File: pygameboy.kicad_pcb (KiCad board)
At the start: 2 copper layers, 49.3 x 59.7 mm, 135 parts, among them J1 Conn_01x01, J2 Conn_01x01, J4 USB_C_Receptacle_USB2.0_16P, J5 MIDI IN, J6 MIDI OUT, Q1 BSS138, SW1 SW_Push, U1 CARTRIDGE, U10 RP2350_80QFN, U2 W25Q128JVS, U5 74x4245, U7 AP2204K-3.3, U8 H11L1, Y1 ABM8-272-T3

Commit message: Ordered!
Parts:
- removed C1, C11, C18, C19, C20, C21, C22, C23, C24, C25, C26, C27: 100n, Capacitor_SMD:C_0402_1005Metric
- removed the C13 at (134.0, 72.9)
- removed C14, C15: 4.7u, Capacitor_SMD:C_0402_1005Metric
- removed C3, C4: 15p, Capacitor_SMD:C_0402_1005Metric
- removed C6: 4.7u, RP2350_80QFN_minimal:C_0402_1005Metric_small_pads
- removed the C7 at (189.7, 39.5)
- removed L1: 3.3u, RP2350_80QFN_minimal:L_pol_2016
- removed R12: DNF, Resistor_SMD:R_0402_1005Metric
- removed R14, R16: 1k, Resistor_SMD:R_0402_1005Metric
- removed R15: 33, Resistor_SMD:R_0402_1005Metric
- removed R17, R18: 27, Resistor_SMD:R_0402_1005Metric
- removed the R2 at (185.4, 45.5)
- removed the R3 at (185.7, 41.1)
- removed TP36: SAMD_RESET, keystone:5015-SMT-TestPoint
- removed Y1: ABM8-272-T3, Crystal:Crystal_SMD_3225-4Pin_3.2x2.5mm
- added C2: 47uF, Capacitor_SMD:C_0805_2012Metric, F.Cu at (146.3, 65.2)
- added C201: 100n, Capacitor_SMD:C_0402_1005Metric, F.Cu at (133.8, 50.6)
- added C202: 15p, Capacitor_SMD:C_0402_1005Metric, F.Cu at (133.9, 75.0)
- added C203: 15p, Capacitor_SMD:C_0402_1005Metric, F.Cu at (136.9, 75.0)
- added C204: 4.7u, RP2350_80QFN_minimal:C_0402_1005Metric_small_pads, F.Cu at (138.3, 58.5)
- added C205: 4.7u, RP2350_80QFN_minimal:C_0402_1005Metric_small_pads, F.Cu at (138.3, 57.5)
- added C206: 100n, Capacitor_SMD:C_0402_1005Metric, F.Cu at (143.3, 64.1)
- added C207: 4.7u, Capacitor_SMD:C_0402_1005Metric, F.Cu at (140.6, 57.8)
- added C210: 100n, Capacitor_SMD:C_0402_1005Metric, F.Cu at (142.9, 60.3)
- added C212: 100n, Capacitor_SMD:C_0402_1005Metric, F.Cu at (141.8, 70.5)
- added C214: 100n, Capacitor_SMD:C_0402_1005Metric, F.Cu at (129.1, 56.0)
- added C215: 100n, Capacitor_SMD:C_0402_1005Metric, F.Cu at (127.3, 61.7)
- added C216: 100n, Capacitor_SMD:C_0402_1005Metric, F.Cu at (134.2, 55.8)
- added C217: 100n, Capacitor_SMD:C_0402_1005Metric, F.Cu at (134.2, 71.3)
- added C218: 100n, Capacitor_SMD:C_0402_1005Metric, F.Cu at (132.7, 71.3)
- added J14: Conn_01x04, Connector_JST:JST_SH_SM04B-SRSS-TB_1x04-1MP_P1.00mm_Horizontal, F.Cu at (138.0, 41.5)
- added L201: 3.3u, RP2350_80QFN_minimal:L_pol_2016, F.Cu at (138.3, 56.0)
- added R11: 10k, Resistor_SMD:R_0402_1005Metric, F.Cu at (146.8, 83.8)
- added R201: 10k, Resistor_SMD:R_0402_1005Metric, F.Cu at (124.8, 48.4)
- added R202: 1k, Resistor_SMD:R_0402_1005Metric, F.Cu at (135.6, 72.9)
- added R203: 33, Resistor_SMD:R_0402_1005Metric, F.Cu at (140.6, 55.9)
- added R204: 1k, Resistor_SMD:R_0402_1005Metric, F.Cu at (146.1, 51.4)
- added SW2: SW_Push, Button_Switch_SMD:SW_SPST_TS-1088-xR020, F.Cu at (147.2, 45.6)
- added Y201: ABM8-272-T3, Crystal:Crystal_SMD_3225-4Pin_3.2x2.5mm, F.Cu at (135.3, 78.6)
- C10, C13: footprint Capacitor_SMD:C_0603_1608Metric_Pad1.08x0.95mm_HandSolder -> Capacitor_SMD:C_0402_1005Metric
- C16, C17: value C_Small -> 100n; footprint Capacitor_SMD:C_0603_1608Metric_Pad1.08x0.95mm_HandSolder -> Capacitor_SMD:C_0402_1005Metric
- C7: value 4.7u -> 100n; footprint RP2350_80QFN_minimal:C_0402_1005Metric_small_pads -> Capacitor_SMD:C_0402_1005Metric
- C8: value 0.1uF -> 100n; footprint Capacitor_SMD:C_0603_1608Metric_Pad1.08x0.95mm_HandSolder -> Capacitor_SMD:C_0402_1005Metric
- D3: footprint LED_SMD:LED_0805_2012Metric_Pad1.15x1.40mm_HandSolder -> LED_SMD:LED_0603_1608Metric
- J5: value MIDI IN -> AudioJack4; footprint adafruit:4UCONN_19269_TRS -> Connector_Audio:Jack_3.5mm_PJ320D_Horizontal
- J6: value MIDI OUT -> AudioJack4; footprint adafruit:4UCONN_19269_TRS -> Connector_Audio:Jack_3.5mm_PJ320D_Horizontal
- Q1: footprint TO_SOT_Packages_SMD:SOT-23 -> Package_TO_SOT_SMD:SOT-23
- R1, R5, R8: footprint Resistor_SMD:R_0603_1608Metric_Pad0.98x0.95mm_HandSolder -> Resistor_SMD:R_0402_1005Metric
- R10: value 0 -> 5.1k
- R2: value 1k -> 10k
- R3: value 33 -> 10k
- R4: value 1k -> 5.1k; footprint Resistor_SMD:R_0603_1608Metric_Pad0.98x0.95mm_HandSolder -> Resistor_SMD:R_0402_1005Metric
- R6, R7: footprint Resistor_SMD:R_0603_1608Metric_Pad0.98x0.95mm_HandSolder -> Resistor_SMD:R_0603_1608Metric
- R9: value DNF -> 5.1k
- SW1: footprint Button_Switch_SMD:SW_SPST_KMR2 -> Button_Switch_SMD:SW_SPST_TS-1088-xR020
- moved R10 67.3 mm to (125.8, 47.4), turned to 180 degrees
- moved R9 63.6 mm to (129.6, 46.8), turned to 180 degrees
- moved C8 58.5 mm to (138.3, 74.0), turned to 180 degrees
- moved Q1 43.7 mm to (144.8, 68.2), turned to 180 degrees
- moved FID0 30.4 mm to (137.9, 47.4)
- moved C7 24.8 mm to (139.1, 82.3), turned to 180 degrees
- moved R1 22.0 mm to (142.7, 51.9), turned to 0 degrees
- moved C16 18.9 mm to (144.6, 51.9), turned to 0 degrees
- moved R3 16.3 mm to (138.8, 72.5), turned to 90 degrees
- moved R2 12.5 mm to (147.2, 68.7)
- moved R7 12.1 mm to (127.8, 56.5), turned to 135 degrees
- moved D1 8.90 mm to (119.5, 54.0)
- moved J5 7.62 mm to (105.7, 45.5)
- moved J6 7.62 mm to (116.4, 45.5)
- moved C209 4.94 mm to (122.4, 64.3)
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- renumbered C10 to C208, C8 to C209, C16 to C211, C17 to C213, R7 to R205, R8 to R206, U2 to U201, U10 to U202
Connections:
- C16 pad 1: /SAMD_RESET -> /RESET
- C7 pad 1: +1V1 -> +5V
- J4 pad A5: unconnected-(J4-CC1-PadA5) -> Net-(J4-CC1)
- J4 pad B5: unconnected-(J4-CC2-PadB5) -> Net-(J4-CC2)
- Q1 pad 1: /GB_RESET -> /RP_GB_RESET
- Q1 pad 3: /RESET -> /GB_RESET
- R1 pad 2: /SAMD_RESET -> /RESET
- R10 pad 1: /RP2350 Core/QSPI_SS -> GND
- R10 pad 2: /RP2350 Core/FLASH_SS -> Net-(J4-CC2)
- R2 pad 1: /XOUT -> +3V3
- R2 pad 2: Net-(C4-Pad1) -> /RP_GB_RESET
- R205 pad 2: Net-(U1-USB_DP) -> Net-(U202-USB_DP)
- R206 pad 2: Net-(U1-USB_DM) -> Net-(U202-USB_DM)
- R3 pad 2: /VREG_AVDD -> /DATA_OE
- R7 pad 2: Net-(J6-PadR) -> Net-(J6-PadR1)
- R9 pad 1: /MIDI_OUT -> GND
- R9 pad 2: /RP2350 Core/FLASH_SS -> Net-(J4-CC1)
- SW1 pad 1: /SAMD_RESET -> /RESET
- TP30 pad 1: /RESET -> /GB_RESET
- TP77 pad 1: /RESET -> /GB_RESET
- U1 pad 30: /RESET -> /GB_RESET
- U201 pad 1: /RP2350 Core/FLASH_SS -> /BOOT
- U202 pad 35: unconnected-(U10-RUN-Pad35) -> /RESET
- U202 pad 36: /3V_D0 -> /DATA_OE
- U202 pad 37: /3V_D1 -> /3V_D0
- U202 pad 38: /3V_D2 -> /3V_D1
- U202 pad 39: /3V_D3 -> /3V_D2
- U202 pad 40: /3V_D4 -> /3V_D3
- U202 pad 42: /3V_D5 -> /3V_D4
- U202 pad 43: /3V_D6 -> /3V_D5
- U202 pad 44: /3V_D7 -> /3V_D6
- U202 pad 45: /RP2350 Core/GPIO36 -> /3V_D7
- U202 pad 46: /RP2350 Core/GPIO37 -> /RP_GB_RESET
- U202 pad 47: /RP2350 Core/GPIO38 -> /PWM_AUDIO
- U202 pad 56: /RP2350 Core/GPIO45_ADC5 -> /LED
- U202 pad 57: /RP2350 Core/GPIO46_ADC6 -> /SDA
- U202 pad 58: /RP2350 Core/GPIO47_ADC7 -> /SCL
- U202 pad 66: Net-(U10-USB_DM) -> Net-(U202-USB_DM)
- U202 pad 67: Net-(U10-USB_DP) -> Net-(U202-USB_DP)
- U202 pad 75: /RP2350 Core/QSPI_SS -> /BOOT
- U5 pad 2: /3V_RD -> /RD
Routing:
- net +3V3: track 63.0 -> 151.5 mm, vias 1 -> 14
- net /RD: track 11.5 -> 94.1 mm, vias 1 -> 2
- net /CLK: track 13.7 -> 59.9 mm, vias 1 -> 3
- net /WR: track 15.2 -> 60.0 mm
- net /CS: track 14.5 -> 57.0 mm
- net /BOOT: track 0.00 -> 42.2 mm, vias 0 -> 4
- net /A0: track 11.5 -> 52.8 mm
- net /A1: track 15.2 -> 54.6 mm
- net /A2: track 11.5 -> 50.4 mm
- net /MIDI_IN: track 0.00 -> 37.5 mm, vias 0 -> 2
- net /A4: track 12.2 -> 48.3 mm
- net /A3: track 16.8 -> 52.3 mm
- net /GB_RESET: track 0.00 -> 34.9 mm, vias 0 -> 1
- net /A5: track 15.2 -> 49.7 mm
- net +5V: track 51.4 -> 85.1 mm
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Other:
- board size 49.3 x 59.7 mm -> 56 x 60.7 mm
- rule pad_to_mask_clearance: 0.03 -> 0
- board text added: "45"
- board text added: "BEVEL 30"
- board text added: "BOOT"
- board text removed: "${REFERENCE}"
- board text removed: "+3.3V"
- board text removed: "+3V"
- board text removed: "Debug"
- board text removed: "LED"
- board text removed: "SWCLK"
- board text removed: "SWDIO"
- board text removed: "SWO"

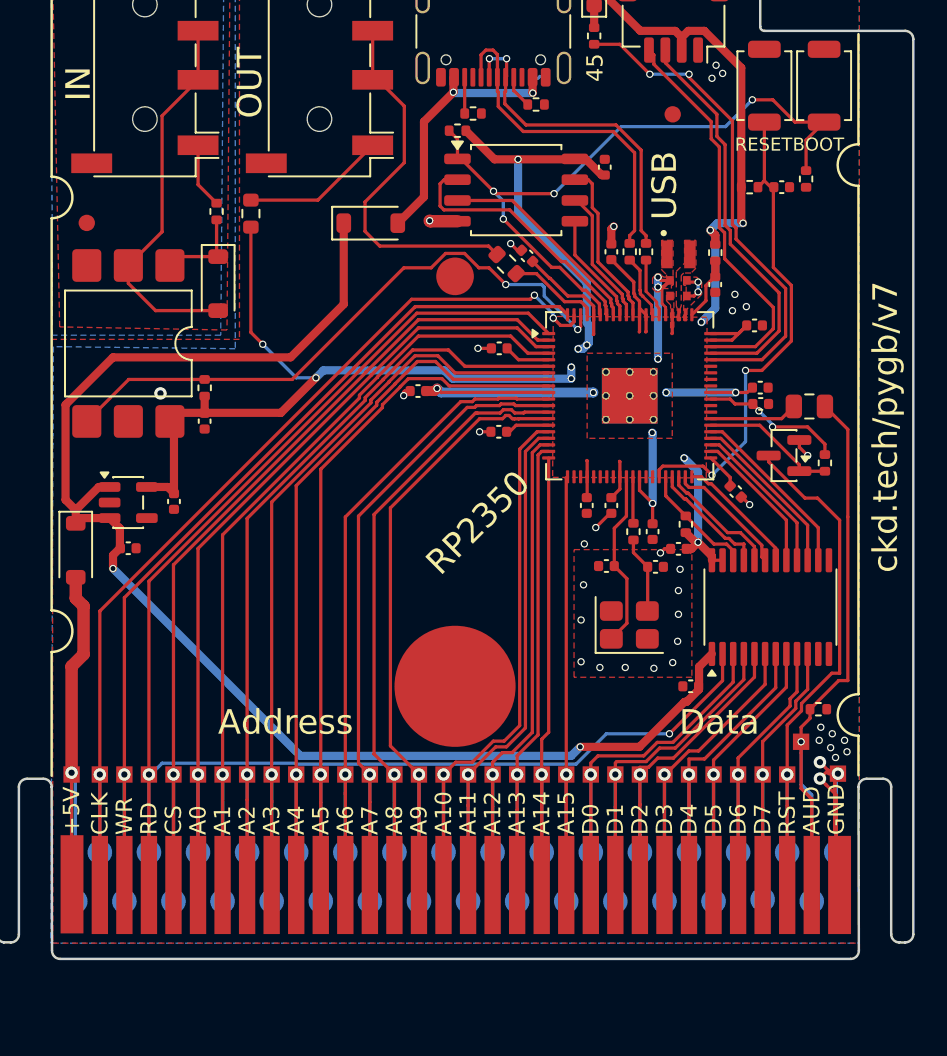
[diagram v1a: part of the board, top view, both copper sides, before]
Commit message: Fix reset circuit. Move control signals to higher pins that both PIO offsets can read. Redo audio circuit
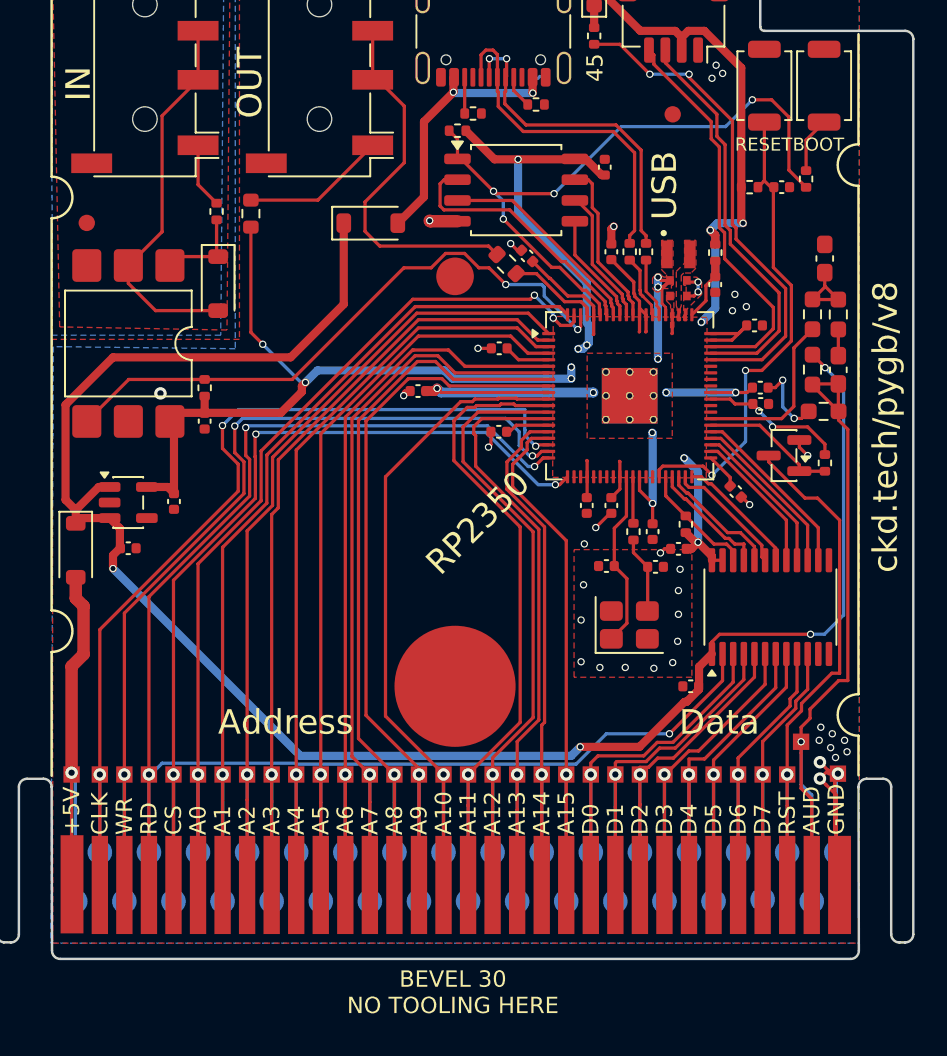
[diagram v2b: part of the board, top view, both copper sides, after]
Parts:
- removed C2: 47uF, Capacitor_SMD:C_0805_2012Metric
- removed R11: 10k, Resistor_SMD:R_0402_1005Metric
- added C101: 1u, Capacitor_SMD:C_0603_1608Metric_Pad1.08x0.95mm_HandSolder, F.Cu at (148.1, 63.0)
- added C102: 100n, Capacitor_SMD:C_0603_1608Metric_Pad1.08x0.95mm_HandSolder, F.Cu at (147.2, 56.2)
- added R101: 1k, Resistor_SMD:R_0603_1608Metric_Pad0.98x0.95mm_HandSolder, F.Cu at (146.5, 59.6)
- added R102: 10k, Resistor_SMD:R_0603_1608Metric_Pad0.98x0.95mm_HandSolder, F.Cu at (148.1, 59.6)
- added R103: 5.6k, Resistor_SMD:R_0603_1608Metric_Pad0.98x0.95mm_HandSolder, F.Cu at (146.5, 63.0)
- added R104: 4.7k, Resistor_SMD:R_0603_1608Metric_Pad0.98x0.95mm_HandSolder, F.Cu at (147.2, 65.5)
- turned R204 to 90 degrees
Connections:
- R201 pad 2: /BOOT -> /RP2350 Core/QSPI_SS
- R204 pad 1: /BOOT -> /RP2350 Core/QSPI_SS
- R204 pad 2: GND -> /BOOT
- U201 pad 1: /BOOT -> /RP2350 Core/QSPI_SS
- U202 pad 1: /RD -> /A2
- U202 pad 11: /A6 -> /A10
- U202 pad 12: /A7 -> /A11
- U202 pad 13: /A8 -> /A12
- U202 pad 14: /A9 -> /A13
- U202 pad 16: /A10 -> /A14
- U202 pad 17: /A11 -> /A15
- U202 pad 18: /A12 -> /CLK
- U202 pad 19: /A13 -> /WR
- U202 pad 2: /CS -> /A3
- U202 pad 20: /A14 -> /RD
- U202 pad 21: /A15 -> /CS
- U202 pad 3: /A0 -> /A4
- U202 pad 4: /A1 -> /A5
- U202 pad 6: /A2 -> /A6
- U202 pad 7: /A3 -> /A7
- U202 pad 75: /BOOT -> /RP2350 Core/QSPI_SS
- U202 pad 79: /CLK -> /A0
- U202 pad 8: /A4 -> /A8
- U202 pad 80: /WR -> /A1
- U202 pad 9: /A5 -> /A9
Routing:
- net /RP2350 Core/QSPI_SS: track 0.00 -> 41.3 mm, vias 0 -> 4
- net /BOOT: track 42.2 -> 3.42 mm, vias 4 -> 0
- net +5V: track 85.1 -> 111.3 mm, vias 2 -> 4
- net /A11: track 37.8 -> 45.4 mm
- net /A13: track 35.3 -> 42.7 mm
- net /A12: track 36.2 -> 43.6 mm
- net /A10: track 36.5 -> 43.1 mm
- net /A8: track 41.3 -> 47.6 mm
- net /A9: track 43.6 -> 49.9 mm
- net /A7: track 45.1 -> 50.7 mm
- net /A15: track 32.7 -> 37.9 mm
- net /PWM_AUDIO: track 5.39 -> 10.6 mm
- net /A6: track 42.7 -> 47.9 mm
- net GND: track 36.5 -> 41.6 mm, vias 41 -> 43
- net /AUD: track 41.6 -> 46.5 mm
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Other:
- board text added: "BEVEL 30 NO TOOLING HERE"
- board text added: "ckd.tech/pygb/v8"
- board text removed: "BEVEL 30"
- board text removed: "ckd.tech/pygb/v7"
